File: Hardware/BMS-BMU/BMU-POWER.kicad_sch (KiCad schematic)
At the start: 21 parts, among them Q2 AO3401A, U1 TPS54202DDC, U2 TLV75533PDBV

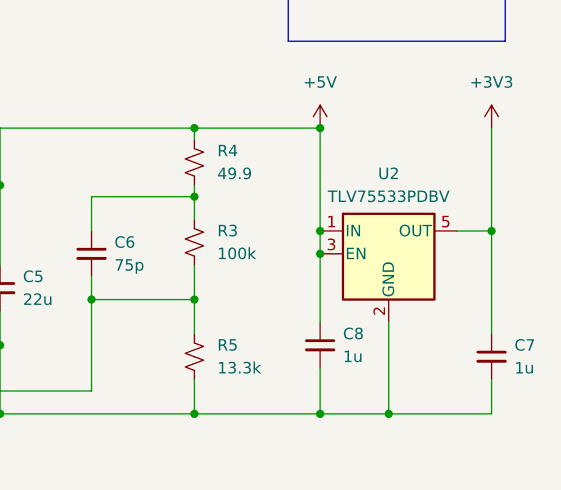
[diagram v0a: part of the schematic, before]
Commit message: update CAN and SHUNT IF
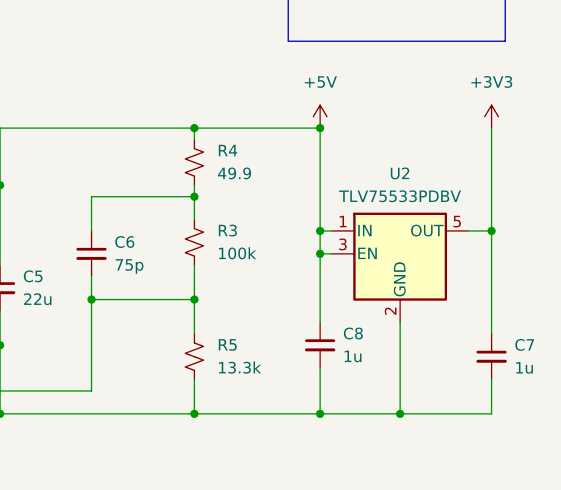
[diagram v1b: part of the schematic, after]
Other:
- moved on the sheet: U2
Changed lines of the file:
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@@
+	)
+	(junction
+		(at 162.56 163.83)
+		(diameter 0)
+		(color 0 0 0 0)
+	)
+	(junction
+		(at 135.89 135.89)
+		(diameter 0)
+		(color 0 0 0 0)
+	)
+	(junction
+		(at 287.02 163.83)
+		(diameter 0)
+		(color 0 0 0 0)
+	)
+	(junction
+		(at 204.47 163.83)
+		(diameter 0)
+		(color 0 0 0 0)
+	)
+	(junction
+		(at 242.57 138.43)
+		(diameter 0)
+		(color 0 0 0 0)
+	)
+	(junction
+		(at 264.16 132.08)
+		(diameter 0)
+		(color 0 0 0 0)
+	)
+	(junction
+		(at 226.06 138.43)
+		(diameter 0)
+		(color 0 0 0 0)
+	)
+	(junction
+		(at 252.73 151.13)
+		(diameter 0)
+		(color 0 0 0 0)
+	)
+	(junction
+		(at 171.45 135.89)
+		(diameter 0)
+		(color 0 0 0 0)
+	)
+	(junction
+		(at 181.61 135.89)
+		(diameter 0)
+		(color 0 0 0 0)
 	)
 	(junction
@@
 	)
 	(junction
+		(at 264.16 163.83)
+		(diameter 0)
+		(color 0 0 0 0)
+	)
+	(junction
+		(at 162.56 135.89)
+		(diameter 0)
+		(color 0 0 0 0)
+	)
+	(junction
+		(at 242.57 156.21)
+		(diameter 0)
+		(color 0 0 0 0)
+	)
+	(junction
+		(at 233.68 138.43)
+		(diameter 0)
+		(color 0 0 0 0)
+	)
+	(junction
 		(at 297.18 143.51)
 		(diameter 0)
@@
 	)
 	(junction
-		(at 162.56 163.83)
-		(diameter 0)
-		(color 0 0 0 0)
-	)
-	(junction
-		(at 135.89 135.89)
-		(diameter 0)
-		(color 0 0 0 0)
-	)
-	(junction
-		(at 204.47 163.83)
-		(diameter 0)
-		(color 0 0 0 0)
-	)
-	(junction
-		(at 242.57 138.43)
+		(at 264.16 151.13)
+		(diameter 0)
+		(color 0 0 0 0)
+	)
+	(junction
+		(at 148.59 147.32)
+		(diameter 0)
+		(color 0 0 0 0)
+	)
+	(junction
+		(at 181.61 149.86)
+		(diameter 0)
+		(color 0 0 0 0)
+	)
+	(junction
+		(at 148.59 163.83)
+		(diameter 0)
+		(color 0 0 0 0)
+	)
+	(junction
+		(at 278.13 132.08)
+		(diameter 0)
+		(color 0 0 0 0)
+	)
+	(junction
+		(at 242.57 163.83)
+		(diameter 0)
+		(color 0 0 0 0)
+	)
+	(junction
+		(at 171.45 163.83)
+		(diameter 0)
+		(color 0 0 0 0)
+	)
+	(junction
+		(at 125.73 135.89)
 		(diameter 0)
 		(color 0 0 0 0)
@@
 	)
 	(junction
-		(at 285.75 163.83)
-		(diameter 0)
-		(color 0 0 0 0)
-	)
-	(junction
-		(at 264.16 132.08)
-		(diameter 0)
-		(color 0 0 0 0)
-	)
-	(junction
-		(at 226.06 138.43)
-		(diameter 0)
-		(color 0 0 0 0)
-	)
-	(junction
-		(at 252.73 151.13)
-		(diameter 0)
-		(color 0 0 0 0)
-	)
-	(junction
-		(at 171.45 135.89)
-		(diameter 0)
-		(color 0 0 0 0)
-	)
-	(junction
-		(at 181.61 135.89)
-		(diameter 0)
-		(color 0 0 0 0)
-	)
-	(junction
-		(at 264.16 163.83)
-		(diameter 0)
-		(color 0 0 0 0)
-	)
-	(junction
-		(at 162.56 135.89)
-		(diameter 0)
-		(color 0 0 0 0)
-	)
-	(junction
-		(at 242.57 156.21)
-		(diameter 0)
-		(color 0 0 0 0)
-	)
-	(junction
-		(at 233.68 138.43)
-		(diameter 0)
-		(color 0 0 0 0)
-	)
-	(junction
-		(at 264.16 151.13)
-		(diameter 0)
-		(color 0 0 0 0)
-	)
-	(junction
-		(at 148.59 147.32)
-		(diameter 0)
-		(color 0 0 0 0)
-	)
-	(junction
-		(at 181.61 149.86)
-		(diameter 0)
-		(color 0 0 0 0)
-	)
-	(junction
-		(at 148.59 163.83)
-		(diameter 0)
-		(color 0 0 0 0)
-	)
-	(junction
-		(at 278.13 132.08)
-		(diameter 0)
-		(color 0 0 0 0)
-	)
-	(junction
-		(at 242.57 163.83)
-		(diameter 0)
-		(color 0 0 0 0)
-	)
-	(junction
-		(at 171.45 163.83)
-		(diameter 0)
-		(color 0 0 0 0)
-	)
-	(junction
-		(at 125.73 135.89)
-		(diameter 0)
-		(color 0 0 0 0)
-	)
-	(junction
 		(at 264.16 139.7)
 		(diameter 0)
@@
 	(wire
 		(pts
-			(xy 285.75 153.67) (xy 285.75 163.83)
+			(xy 287.02 153.67) (xy 287.02 163.83)
 		)
 		(stroke
@@
 	(wire
 		(pts
+			(xy 279.4 146.05) (xy 278.13 146.05)
+		)
+		(stroke
+			(width 0)
+			(type default)
+		)
+	)
+	(wire
+		(pts
 			(xy 297.18 143.51) (xy 297.18 154.94)
 		)
@@
 	(wire
 		(pts
-			(xy 285.75 163.83) (xy 297.18 163.83)
-		)
-		(stroke
-			(width 0)
-			(type default)
-		)
-	)
-	(wire
-		(pts
-			(xy 278.13 163.83) (xy 285.75 163.83)
+			(xy 278.13 163.83) (xy 287.02 163.83)
 		)
 		(stroke
@@
 	(wire
 		(pts
-			(xy 297.18 143.51) (xy 293.37 143.51)
+			(xy 297.18 143.51) (xy 294.64 143.51)
 		)
 		(stroke
@@
 	(wire
 		(pts
+			(xy 287.02 163.83) (xy 297.18 163.83)
+		)
+		(stroke
+			(width 0)
+			(type default)
+		)
+	)
+	(wire
+		(pts
 			(xy 264.16 132.08) (xy 264.16 133.35)
 		)
@@
 		(pts
 			(xy 162.56 148.59) (xy 162.56 163.83)
+		)
+		(stroke
+			(width 0)
+			(type default)
+		)
+	)
+	(wire
+		(pts
+			(xy 279.4 143.51) (xy 278.13 143.51)
 		)
 		(stroke
@@
 	(symbol
 		(lib_id "Regulator_Linear:TLV75533PDBV")
-		(at 285.75 146.05 0)
+		(at 287.02 146.05 0)
 		(unit 1)
 		(body_style 1)
@@
 		(fields_autoplaced yes)
 		(property "Reference" "U2"
-			(at 285.75 137.16 0)
+			(at 287.02 137.16 0)
 			(show_name no)
 			(do_not_autoplace no)
@@
 		)
 		(property "Value" "TLV75533PDBV"
-			(at 285.75 139.7 0)
+			(at 287.02 139.7 0)
 			(show_name no)
 			(do_not_autoplace no)
@@
 		)
 		(property "Footprint" "Package_TO_SOT_SMD:SOT-23-5"
-			(at 285.75 137.795 0)
+			(at 287.02 137.795 0)
 			(hide yes)
 			(show_name no)
@@
 		)
 		(property "Datasheet" "http://www.ti.com/lit/ds/symlink/tlv755p.pdf"
-			(at 285.75 144.78 0)
+			(at 287.02 144.78 0)
 			(hide yes)
 			(show_name no)
@@
 		)
 		(property "Description" "500mA Low Dropout Voltage Regulator, Fixed Output 3.3V, SOT-23-5"
-			(at 285.75 146.05 0)
-			(hide yes)
-			(show_name no)
+			(at 287.02 146.05 0)
+			(hide yes)
+			(show_name no)
